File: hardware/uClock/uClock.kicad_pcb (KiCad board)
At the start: 2 copper layers, 27.5 x 27.5 mm, 27 parts, among them J1 USB_B_Micro, J3 SSD1306, Q1 BSS138, Q2 BSS138, Q4 AO3401A, SW1 BUTTON, U1 ESP8285, U2 DS3231MZ, U3 TP4056, U4 CH340C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

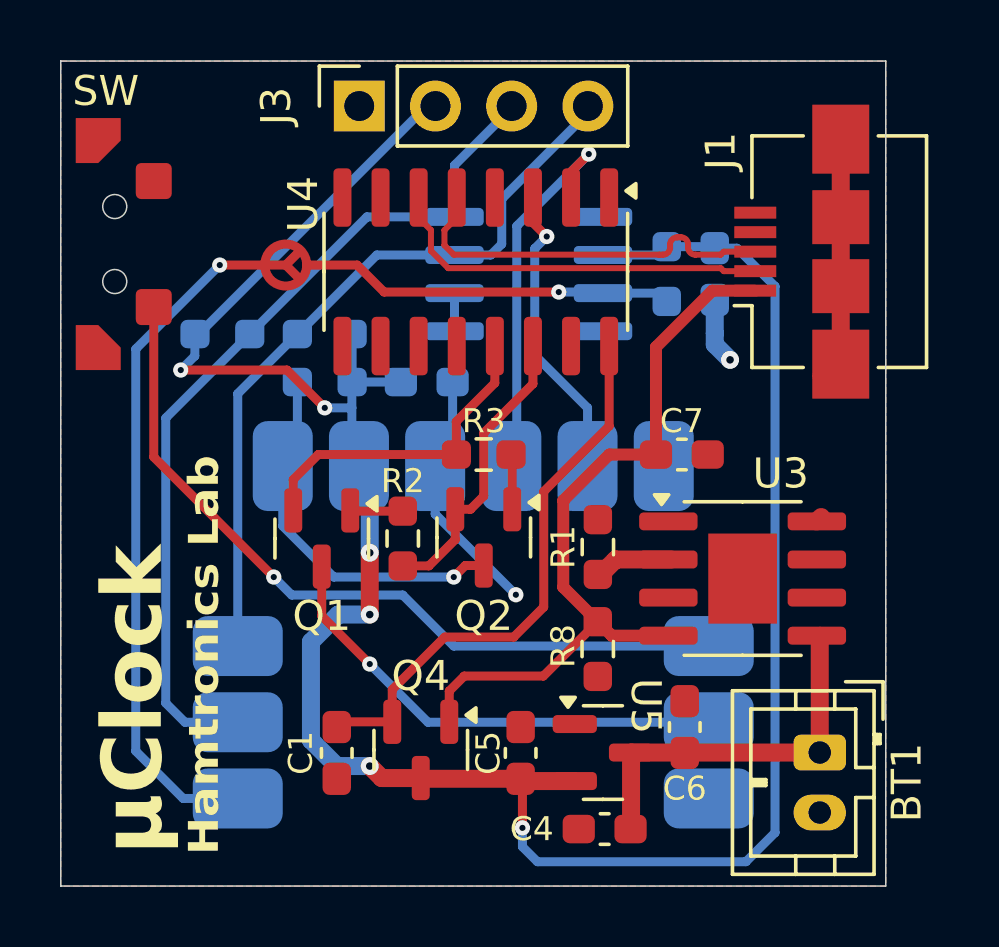
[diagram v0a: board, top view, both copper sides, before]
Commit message: PCB Update - rev2
- CH340 power corrected
- Optimized RTC conspumtion
- Pullup added to SW1
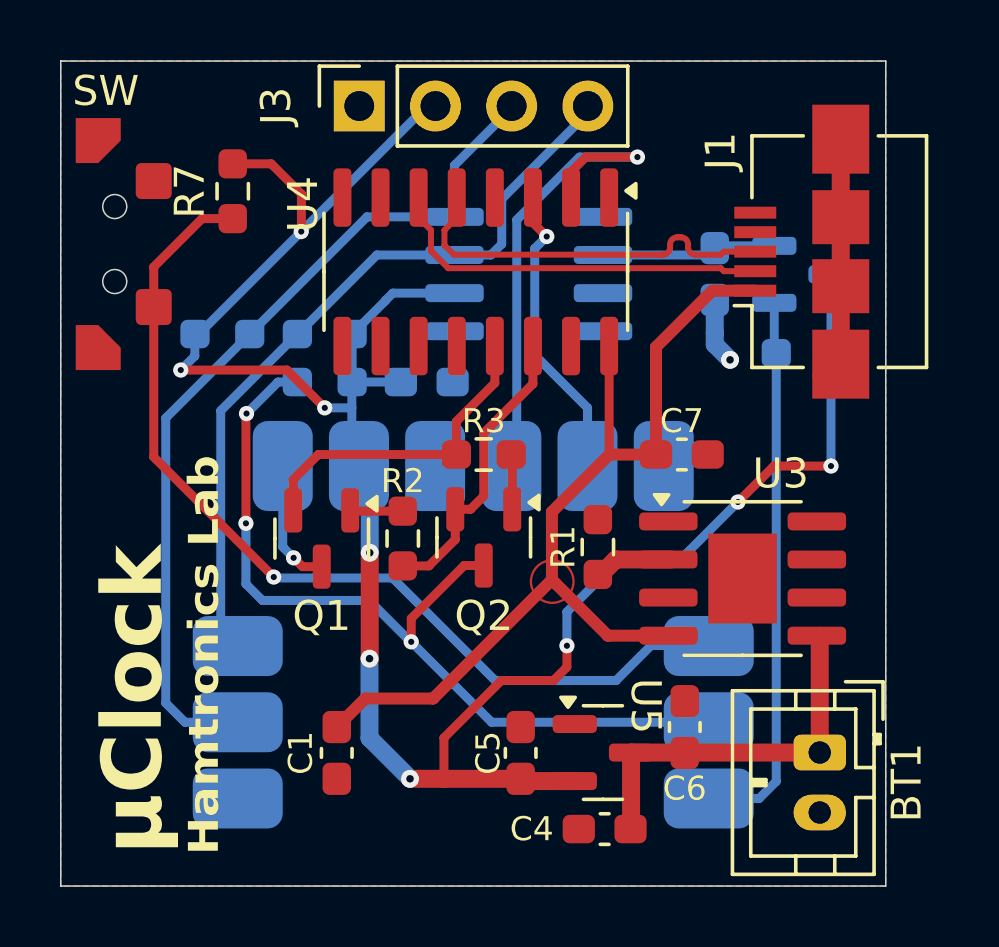
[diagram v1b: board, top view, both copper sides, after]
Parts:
- removed Q4: AO3401A, Package_TO_SOT_SMD:SOT-23
- removed R8: 10k, Resistor_SMD:R_0603_1608Metric_Pad0.98x0.95mm_HandSolder
- added Q5: AO3401A, Package_TO_SOT_SMD:SOT-23, B.Cu at (85.3, 82.1)
- added R7: 10k, Resistor_SMD:R_0603_1608Metric_Pad0.98x0.95mm_HandSolder, F.Cu at (66.3, 79.3)
- moved R9 5.27 mm to (85.3, 84.7), turned to 0 degrees
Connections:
- net /SCL renamed SCL
- net /SDA renamed SDA
- net Net-(Q1-S) renamed DTR
- net Net-(Q2-S) renamed RTS
- C1 pad 1: Net-(Q4-S) -> +5VD
- C3 pad 2: VCC -> Net-(Q5-S)
- Q1 pad 3: Net-(Q1-D) -> ENABLE
- Q2 pad 3: Net-(Q2-D) -> FLASH
- R4 pad 2: Net-(Q2-D) -> FLASH
- R9 pad 1: Net-(U1-IO16) -> RTC_POWER
- U1 pad 1: Net-(Q2-D) -> ENABLE
- U1 pad 10: Net-(U1-IO16) -> unconnected-(U1-IO16-Pad10)
- U1 pad 8: Net-(Q1-D) -> FLASH
- U1 pad 9: unconnected-(U1-IO4-Pad9) -> RTC_POWER
- U2 pad 2: VCC -> Net-(Q5-S)
- U2 pad 3: Net-(U1-IO16) -> unconnected-(U2-~{INT}/SQW-Pad3)
- U2 pad 6: Earth -> VCC
- U4 pad 16: Net-(Q4-S) -> +5VD
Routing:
- net Net-(U1-IO16): track 37.4 -> 0.00 mm, vias 2 -> 0
- net FLASH: track 0.00 -> 29.1 mm, vias 0 -> 3
- net Net-(Q4-S): track 18.8 -> 0.00 mm
- net RTC_POWER: track 0.00 -> 18.5 mm
- net Net-(Q1-D): track 16.0 -> 0.00 mm, vias 1 -> 0
- net Net-(Q2-D): track 12.6 -> 0.00 mm, vias 1 -> 0
- net Earth: track 23.0 -> 12.3 mm, vias 2 -> 1
- net +5VD: track 25.4 -> 31.7 mm
- net Net-(Q5-S): track 0.00 -> 5.91 mm
- net VCC: track 80.9 -> 75.1 mm, vias 6 -> 9
- net Net-(U1-IO2): track 26.4 -> 32.0 mm
- net ENABLE: track 0.00 -> 4.96 mm, vias 0 -> 1
- net Net-(U1-TX0): track 13.2 -> 16.4 mm

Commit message: Updated PCB to REV-3
- Updated PCB traces tolerances from 0.3mm to 0.2mm
- Optimized some traces
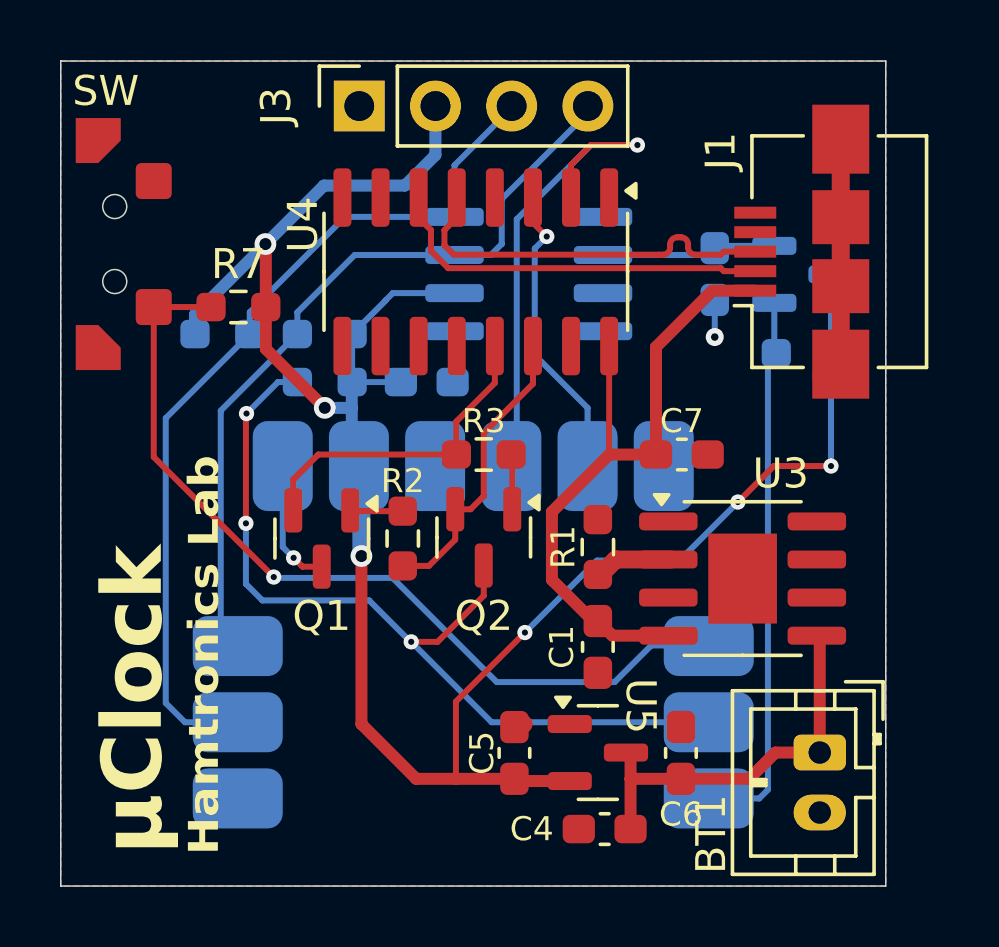
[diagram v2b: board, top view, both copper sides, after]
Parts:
- moved C1 9.39 mm to (78.5, 94.5)
- moved R7 3.86 mm to (66.5, 83.2), turned to 0 degrees
- moved C6 0.87 mm to (81.2, 98.1)
- moved C5 0.21 mm to (75.7, 98.1)
- moved U5 0.17 mm to (78.5, 98.0)
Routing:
- net +5VD: track 31.7 -> 22.5 mm
- net VCC: track 75.1 -> 71.6 mm, vias 9 -> 6
- net Net-(U1-IO2): track 32.0 -> 29.3 mm
- net Earth: track 12.3 -> 10.3 mm
- net +BATT: track 12.8 -> 13.4 mm
